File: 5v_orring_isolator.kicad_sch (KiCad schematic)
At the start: 6 parts, among them U4 TPS2116DRL, U5 TBA2-2411

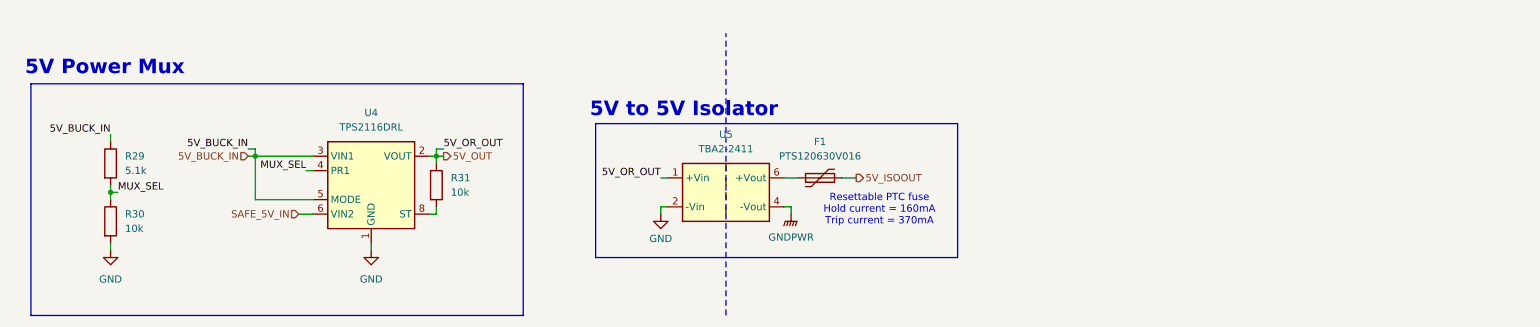
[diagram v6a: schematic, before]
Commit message: redid cypd layout, halfway through 12v buck layout
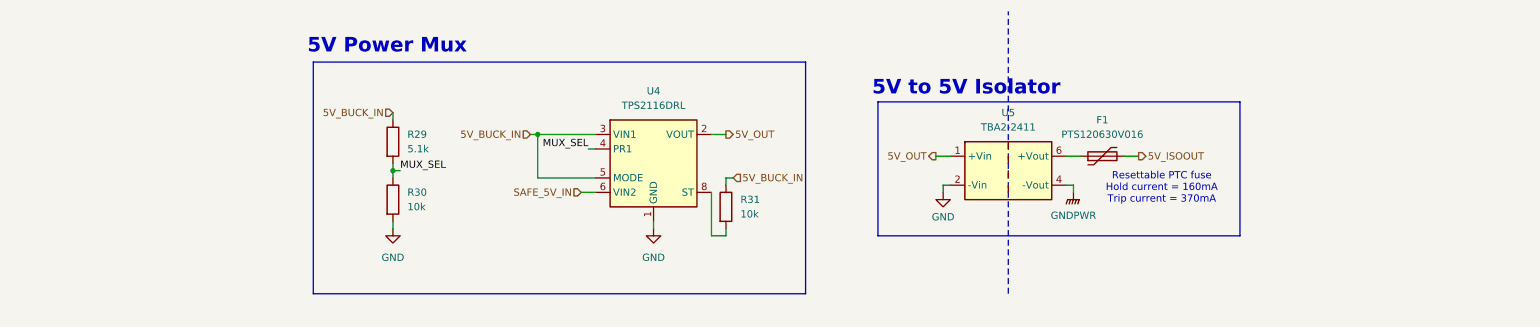
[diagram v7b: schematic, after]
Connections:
- net 5V_BUCK_IN: now also R31.1
- net 5V_OUT: no longer R31.1
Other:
- moved on the sheet: F1, R29, R30, R31, U4, U5

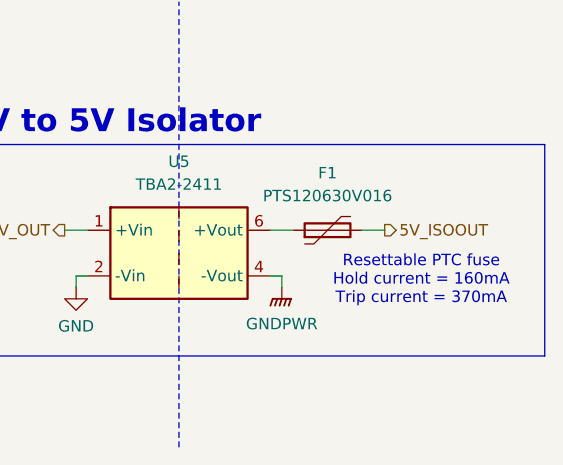
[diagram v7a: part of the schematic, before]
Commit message: fixed clearance violations and made board 3mm shorter
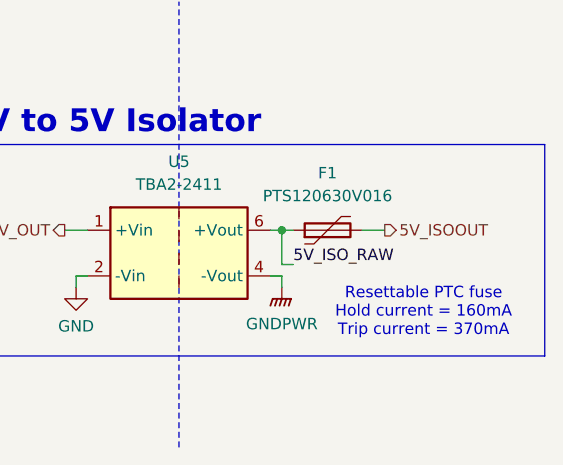
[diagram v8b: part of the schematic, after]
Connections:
- net 5V_ISO_RAW: now reaches F1.1, U5.6 (+Vout)
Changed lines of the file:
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@@
+	)
+	(junction
+		(at 203.2 99.06)
+		(diameter 0)
+		(color 0 0 0 0)
 	)
 	(junction
@@
 	(wire
 		(pts
+			(xy 204.47 102.87) (xy 203.2 102.87)
+		)
+		(stroke
+			(width 0)
+			(type default)
+		)
+	)
+	(wire
+		(pts
 			(xy 212.09 99.06) (xy 214.63 99.06)
 		)
@@
 	(wire
 		(pts
-			(xy 201.93 99.06) (xy 204.47 99.06)
+			(xy 201.93 99.06) (xy 203.2 99.06)
+		)
+		(stroke
+			(width 0)
+			(type default)
+		)
+	)
+	(wire
+		(pts
+			(xy 203.2 102.87) (xy 203.2 99.06)
 		)
 		(stroke
@@
 		(pts
 			(xy 143.51 102.87) (xy 142.24 102.87)
+		)
+		(stroke
+			(width 0)
+			(type default)
+		)
+	)
+	(wire
+		(pts
+			(xy 203.2 99.06) (xy 204.47 99.06)
 		)
 		(stroke
@@
 	(text "Resettable PTC fuse\nHold current = 160mA\nTrip current = 370mA"
 		(exclude_from_sim no)
-		(at 218.694 104.648 0)
+		(at 218.948 108.204 0)
 		(effects
 			(font
@@
 		)
 	)
+	(label "5V_ISO_RAW"
+		(at 204.47 102.87 0)
+		(fields_autoplaced yes)
+		(effects
+			(font
+				(size 1.27 1.27)
+			)
+			(justify left bottom)
+		)
+	)
